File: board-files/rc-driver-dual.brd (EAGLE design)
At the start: 100 x 80 mm, 1 part

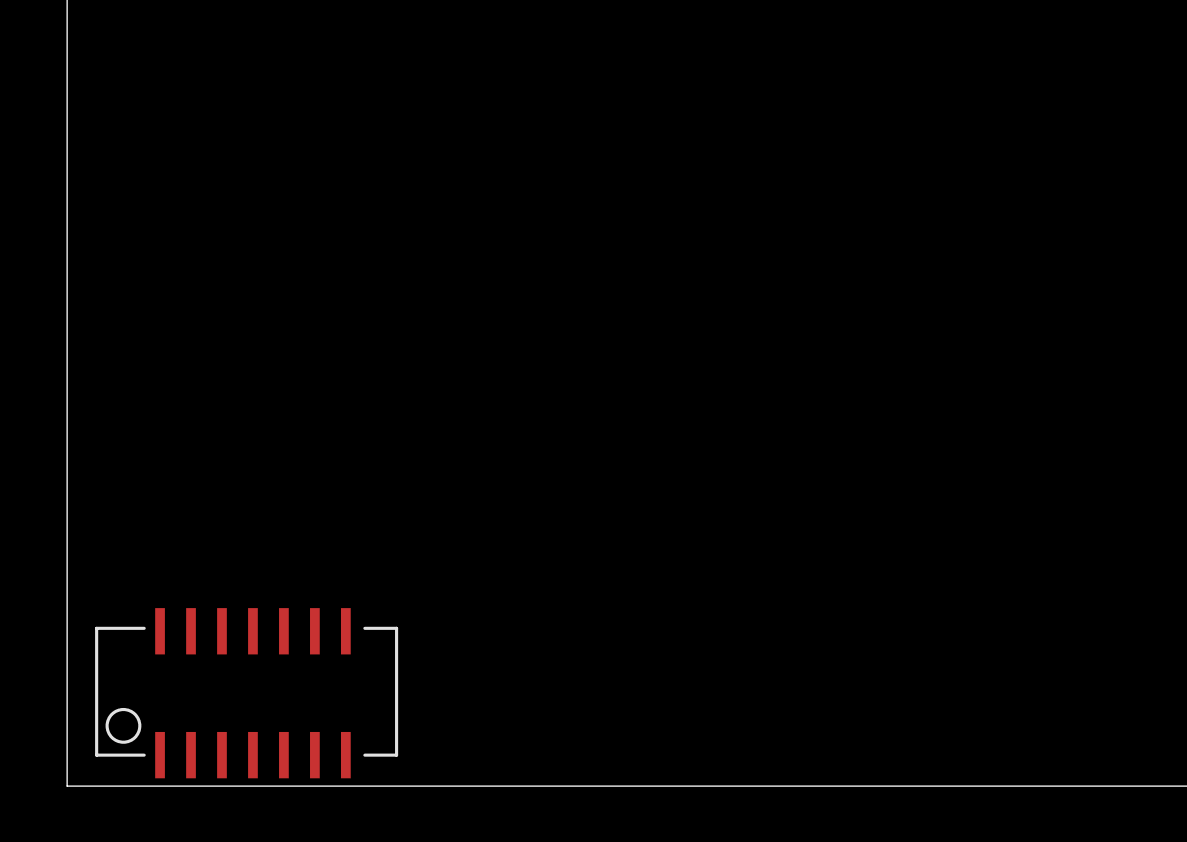
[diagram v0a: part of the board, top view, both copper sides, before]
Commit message: Added motor driver to dual driver board.
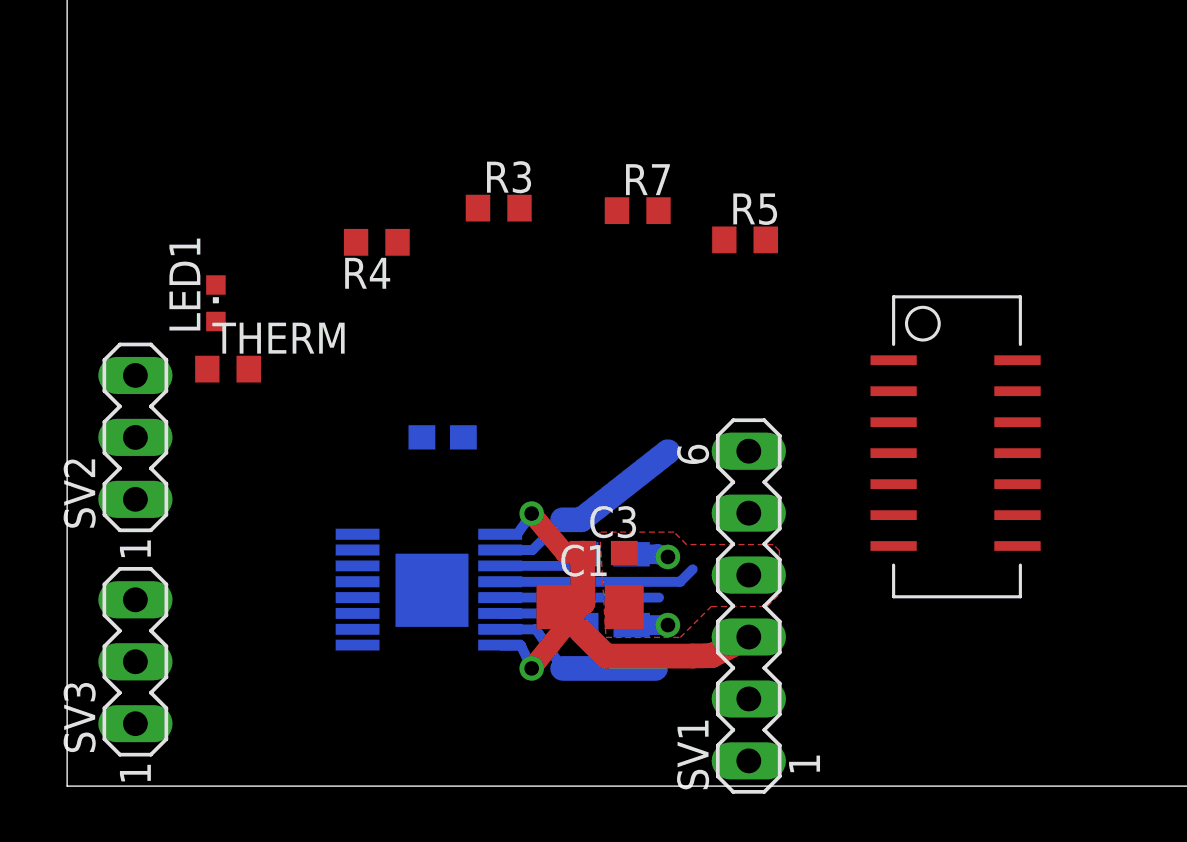
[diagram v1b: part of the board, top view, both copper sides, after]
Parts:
- added C1: 10uf, resistor:C1206
- added C2, C3: 0.1uf, resistor:C0603
- added LED1: (no value), led:CHIPLED_0603
- added R1, R2: (no value), resistor:R0805W
- added R3, R4, R5, R7, THERM: (no value), resistor:R0603
- added SV1: (no value), con-lstb:MA06-1
- added SV2, SV3: (no value), con-lstb:MA03-1
- added U$2: A4954-DUAL-HBRIDGE, rc-parts:TSSOP-16-LP
- moved U$1 32.1 mm to (36.4, 14.9), turned to 270 degrees
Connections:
- new net +5V: C2.1, R3.1, SV2.2, SV3.2, THERM.1, U$1.P$1
- new net GND: C1.2, C2.2, C3.2, LED1.C, R1.2, R2.2, R4.2, R7.2, SV1.4, SV2.3, SV3.3, U$1.P$14, U$2.P$1, U$2.P$17, U$2.P$8
- new net LED: R5.1, U$1.P$10
- new net MOTOR1-1: SV1.1, U$2.P$10
- new net MOTOR1-2: SV1.2, U$2.P$12
- new net MOTOR2-1: SV1.5, U$2.P$13
- new net MOTOR2-2: SV1.6, U$2.P$15
- new net N$1: R1.1, U$2.P$14
- new net N$2: R2.1, U$2.P$11
- new net N$20: U$1.P$9
- new net N$24: U$1.P$4
- new net N$26: U$1.P$3
- new net N$27: U$1.P$2
- new net N$4: LED1.A, R5.2
- new net OUTPUT1: U$1.P$5, U$2.P$6
- new net OUTPUT2: U$1.P$6, U$2.P$5
- new net OUTPUT3: U$1.P$8, U$2.P$3
- new net OUTPUT4: U$1.P$7, U$2.P$4
- new net PWM1: SV2.1, U$1.P$12
- new net PWM2: SV3.1, U$1.P$11
- new net T-OUT: R7.1, THERM.2, U$1.P$13
- new net VM: C1.1, C3.1, SV1.3, U$2.P$16, U$2.P$9
- new net VREF: R3.2, R4.1, U$2.P$2, U$2.P$7
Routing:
- net VM: track 0.00 -> 21.4 mm, vias 0 -> 2
- net MOTOR1-1: track 0.00 -> 8.36 mm
- net MOTOR1-2: track 0.00 -> 8.11 mm
- net MOTOR2-2: track 0.00 -> 7.22 mm
- net MOTOR2-1: track 0.00 -> 6.51 mm
- net N$1: track 0.00 -> 3.48 mm
- net N$2: track 0.00 -> 3.48 mm
- net GND: track 0.00 -> 3.00 mm, vias 0 -> 2
- added copper zone on layer 1, net GND

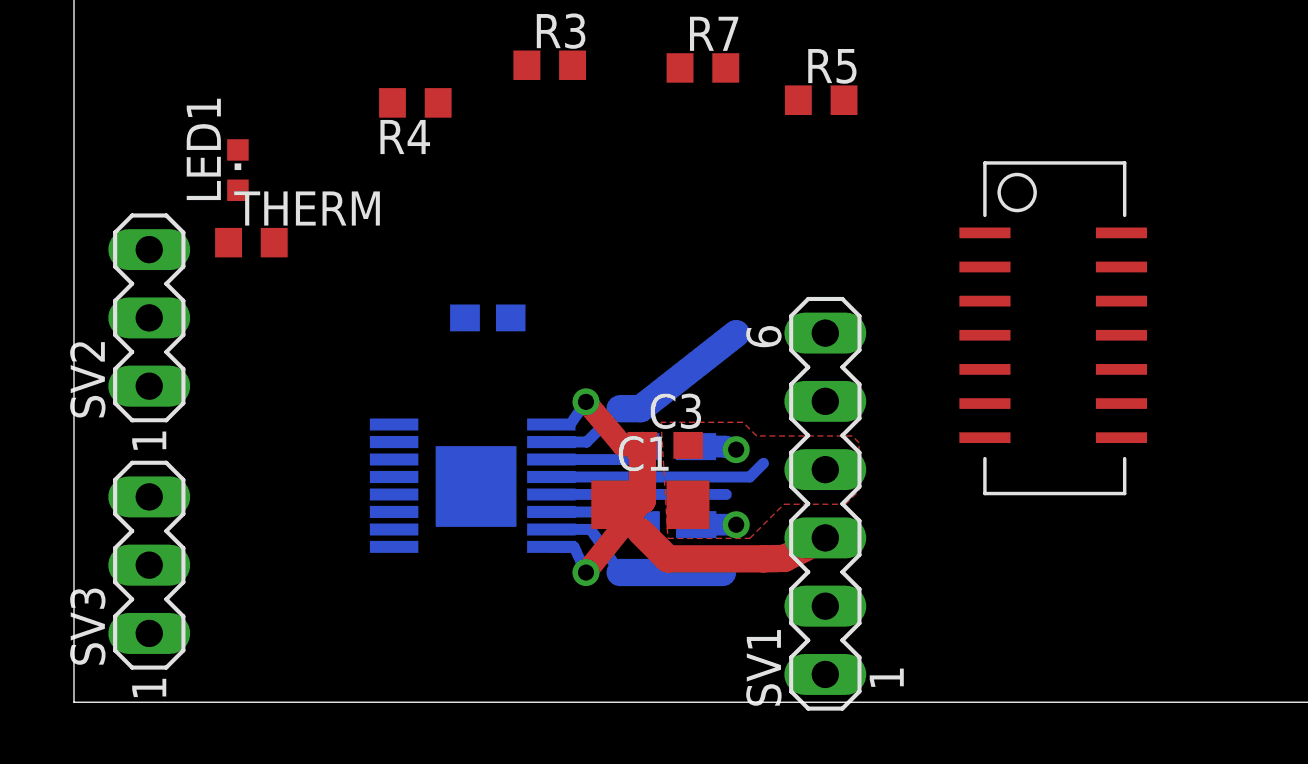
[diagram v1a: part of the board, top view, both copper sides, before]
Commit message: fixing attiny silk. Shortened single rc-driver board.
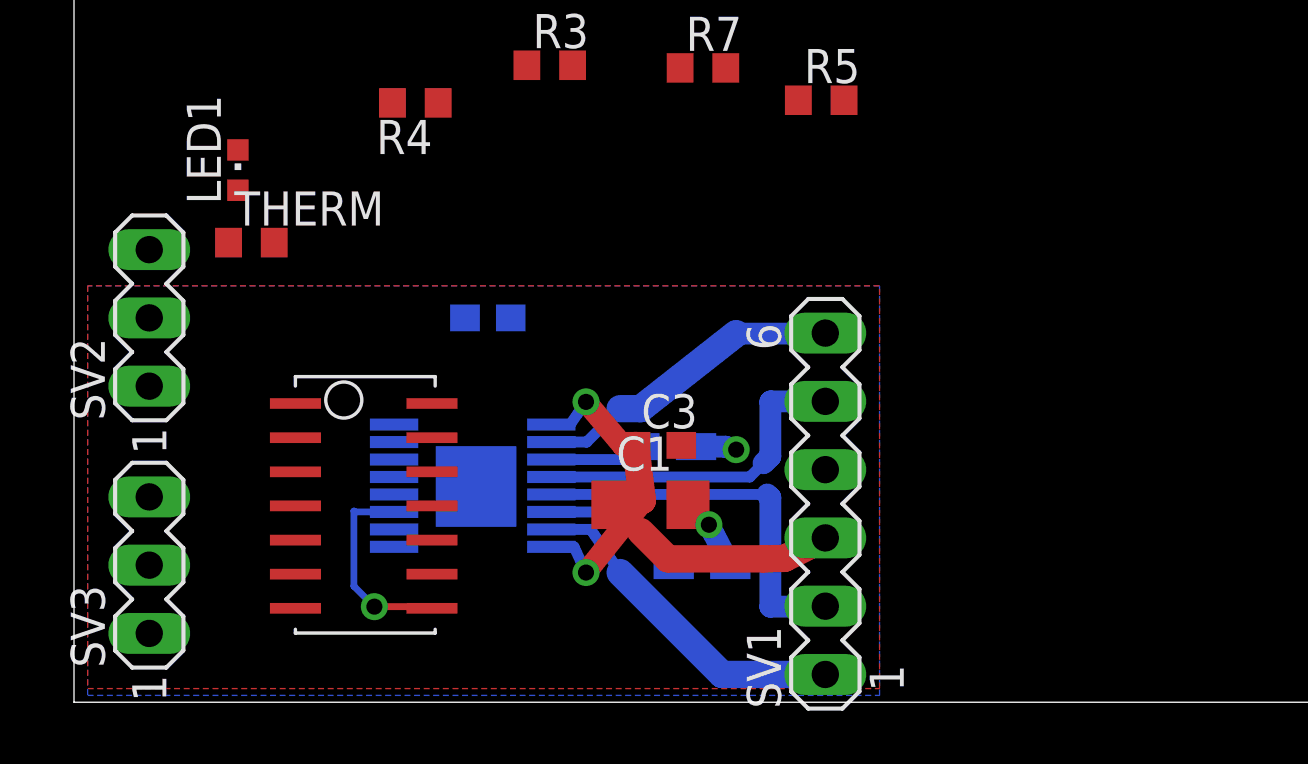
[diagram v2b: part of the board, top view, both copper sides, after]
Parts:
- moved U$1 26.4 mm to (10.8, 8.57)
- moved R1 1.98 mm to (23.4, 5.08)
- moved C3 0.25 mm to (21.7, 9.56)
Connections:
- net MOTOR1-1: now also SV1.6; no longer SV1.1
- net MOTOR1-2: now also SV1.5; no longer SV1.2
- net MOTOR2-1: now also SV1.2; no longer SV1.5
- net MOTOR2-2: now also SV1.1; no longer SV1.6
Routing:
- net MOTOR2-1: track 6.51 -> 14.8 mm
- net OUTPUT3: track 0.00 -> 7.55 mm, vias 0 -> 1
- net MOTOR2-2: track 7.22 -> 12.6 mm
- net MOTOR1-2: track 8.11 -> 12.5 mm
- net MOTOR1-1: track 8.36 -> 11.7 mm
- net N$1: track 3.48 -> 5.46 mm
- added copper zone on layer 16, net GND

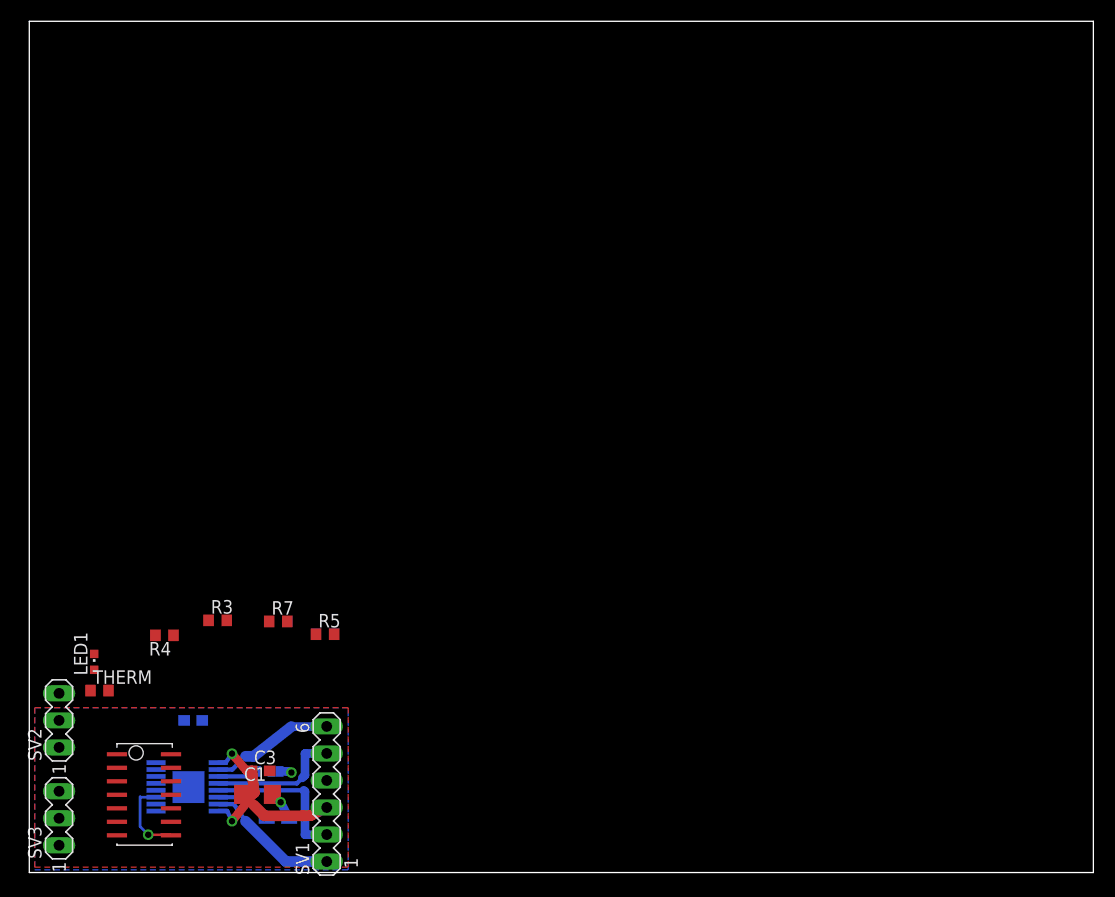
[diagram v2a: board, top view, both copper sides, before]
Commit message: Added license to boards. Finished routingand silks.
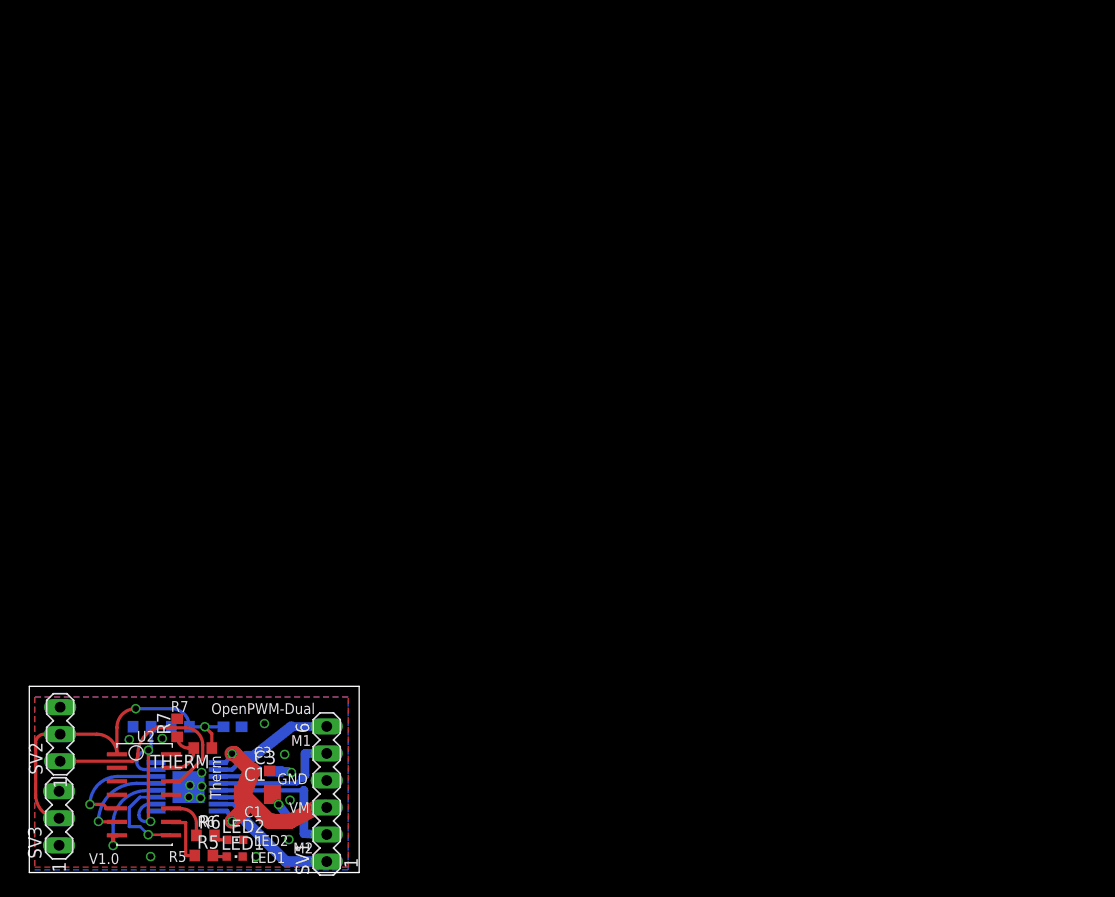
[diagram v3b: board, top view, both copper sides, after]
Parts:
- added LED2: (no value), led:CHIPLED_0603
- added R6: (no value), resistor:R0603
- moved R5 23.7 mm to (16.4, 1.60)
- moved LED1 22.6 mm to (19.3, 1.50), turned to 270 degrees
- moved R7 13.8 mm to (13.9, 13.6), turned to 90 degrees
- moved THERM 11.1 mm to (16.3, 11.7), turned to 180 degrees
- moved R3 10.6 mm to (14.2, 13.7), flipped to the bottom
- moved R4 8.85 mm to (10.6, 13.7), flipped to the bottom, turned to 0 degrees
- moved C2 3.75 mm to (19.1, 13.7), turned to 180 degrees
- moved SV2 1.30 mm to (2.90, 13.0)
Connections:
- removed net N$20: U$1.P$9
- new net LED2: R6.1, U$1.P$10
- new net N$3: LED2.A, R6.2
- new net N$5: U$1.P$11
- net GND: now also LED2.C
- net LED: now also U$1.P$9; no longer U$1.P$10
- net PWM2: no longer U$1.P$11
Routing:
- net +5V: track 0.00 -> 33.0 mm, vias 0 -> 2
- net PWM1: track 0.00 -> 20.8 mm
- net VREF: track 0.00 -> 18.5 mm, vias 0 -> 2
- net OUTPUT1: track 0.00 -> 10.0 mm, vias 0 -> 1
- net OUTPUT4: track 0.00 -> 8.70 mm, vias 0 -> 1
- net OUTPUT2: track 0.00 -> 8.65 mm, vias 0 -> 1
- net LED: track 0.00 -> 5.40 mm
- net T-OUT: track 0.00 -> 5.06 mm
- net LED2: track 0.00 -> 4.08 mm
- net OUTPUT3: track 7.55 -> 8.98 mm
- net N$3: track 0.00 -> 1.37 mm
- net N$4: track 0.00 -> 1.34 mm
- net GND: track 3.23 -> 3.17 mm, vias 2 -> 15
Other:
- board size 100 x 80 mm -> 31 x 17.5 mm
- board text added: "C1"
- board text added: "C2"
- board text added: "C3"
- board text added: "GND"
- board text added: "LED1"
- board text added: "LED2"
- board text added: "M1"
- board text added: "M2"
- board text added: "OpenPWM-Dual"
- board text added: "R1"
- board text added: "R2"
- board text added: "R3"
- board text added: "R4"
- board text added: "R5"
- board text added: "R6"
- board text added: "R7"
- board text added: "Therm"
- board text added: "U2"
- board text added: "V1.0"
- board text added: "VM"

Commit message: add drunken spriral
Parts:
- removed THERM: (no value), resistor:R0603
- added RT1: (no value), resistor:R0603
- moved R1 2.80 mm to (21.1, 6.68)
- moved C3 2.57 mm to (19.2, 9.20)
- moved SV1 1.82 mm to (26.9, 8.89)
- moved C1 1.80 mm to (19.7, 6.74)
- moved R6 1.13 mm to (15.4, 3.62)
- moved C2 1.00 mm to (18.1, 13.7)
- moved LED1 1.00 mm to (18.3, 1.50)
- moved LED2 1.00 mm to (18.4, 3.08)
- moved R2 1.00 mm to (21.1, 9.51)
- moved R3 1.00 mm to (13.2, 13.7)
- moved R4 1.00 mm to (9.60, 13.7)
- moved R7 1.00 mm to (12.9, 13.6)
- moved U$1 1.00 mm to (9.78, 8.57)
- moved U$2 1.00 mm to (14.2, 7.85)
- moved R5 1.00 mm to (15.4, 1.60)
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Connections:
- removed net N$24: U$1.P$4
- removed net N$26: U$1.P$3
- removed net N$27: U$1.P$2
- removed net N$5: U$1.P$11
- net +5V: now also RT1.1; no longer THERM.1
- net PWM2: now also U$1.P$11
- net T-OUT: now also RT1.2; no longer THERM.2
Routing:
- net PWM2: track 0.00 -> 13.2 mm
- net VM: track 21.2 -> 9.96 mm
- net PWM1: track 20.8 -> 10.8 mm
- net VREF: track 18.5 -> 14.1 mm
- net MOTOR2-1: track 14.8 -> 11.6 mm
- net +5V: track 33.0 -> 30.2 mm
- net N$1: track 5.46 -> 3.31 mm
- net MOTOR2-2: track 12.6 -> 11.3 mm
- net LED: track 5.40 -> 4.58 mm
- net OUTPUT3: track 8.98 -> 8.17 mm
- net GND: track 3.17 -> 3.37 mm, vias 15 -> 16
- added copper zone on layer 1, net VM
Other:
- board size 31 x 17.5 mm -> 29.5 x 17.5 mm
- board text added: "RT1"
- board text removed: "Therm"

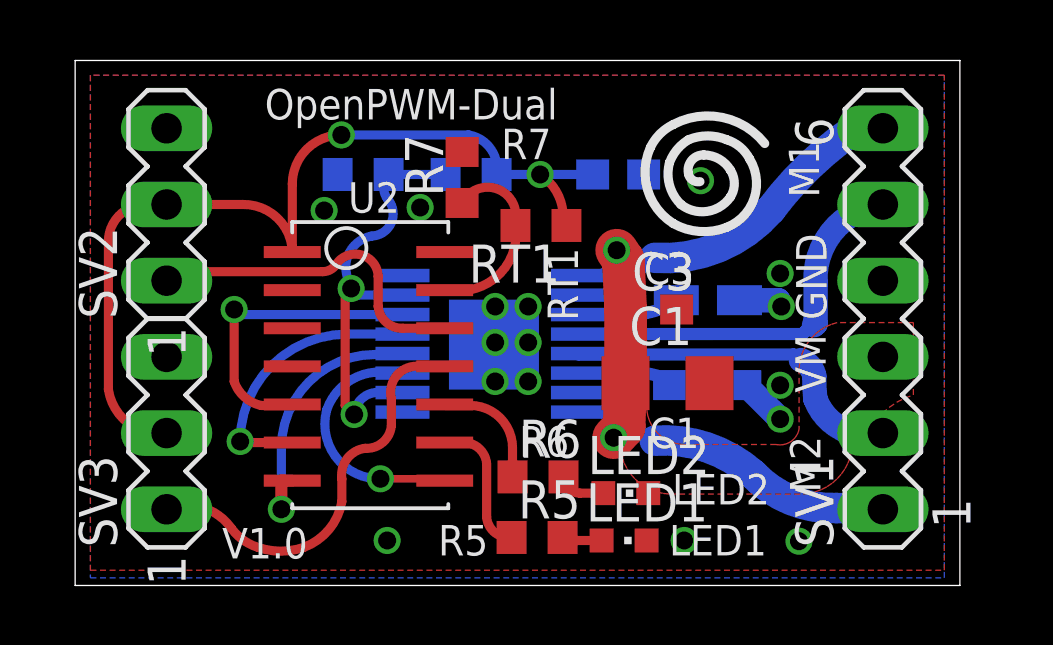
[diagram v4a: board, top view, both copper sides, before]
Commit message: Move squigly lines and extra capacitance on VM.
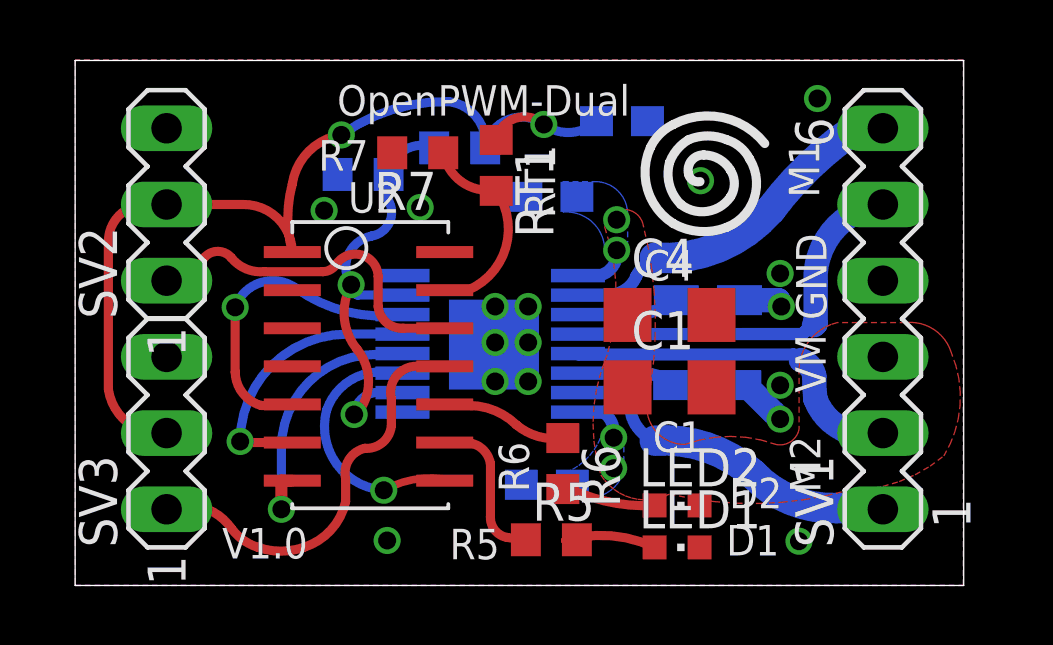
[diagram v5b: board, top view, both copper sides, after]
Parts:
- added C4: 10uf, resistor:C1206
- added C5: 0.1uf, resistor:C0603
- moved C3 6.80 mm to (15.7, 3.36), flipped to the bottom
- moved RT1 2.50 mm to (14.0, 14.0), turned to 270 degrees
- moved C2 1.78 mm to (18.2, 15.5)
- moved LED1 1.78 mm to (20.1, 1.27)
- moved LED2 1.76 mm to (20.1, 2.67)
- moved R7 1.69 mm to (11.4, 14.4), turned to 180 degrees
- moved R3 0.97 mm to (12.8, 14.6)
- moved R6 0.94 mm to (16.3, 4.06), turned to 270 degrees
- moved R5 0.48 mm to (15.9, 1.52)
- moved C1 0.15 mm to (19.8, 6.60)
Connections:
- net GND: now also C4.2, C5.2
- net VM: now also C4.1, C5.1
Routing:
- net VM: track 9.96 -> 3.50 mm, vias 2 -> 4
- net N$4: track 1.34 -> 3.35 mm
- net N$3: track 1.55 -> 3.11 mm
- net T-OUT: track 5.38 -> 6.49 mm
- added copper zone on layer 16, net VM
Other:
- board size 29.5 x 17.5 mm -> 29.6 x 17.5 mm
- board text added: "C4"
- board text added: "C5"
- board text added: "D1"
- board text added: "D2"
- board text removed: "LED1"
- board text removed: "LED2"
